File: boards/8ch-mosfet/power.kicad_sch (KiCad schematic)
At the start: 21 parts, among them J3 Screw_Terminal_01x08, J4 Screw_Terminal_01x08, U3 R-78K5.0-1.0

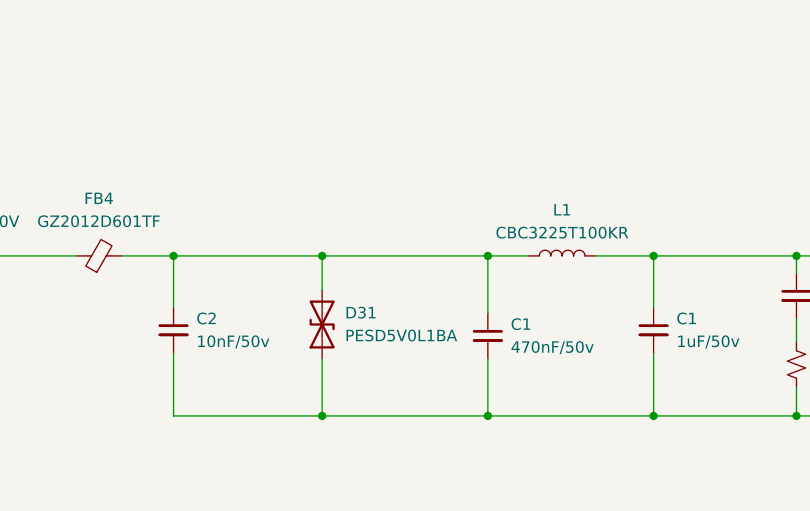
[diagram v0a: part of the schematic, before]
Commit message: added in reverse polarity diode to power circuit
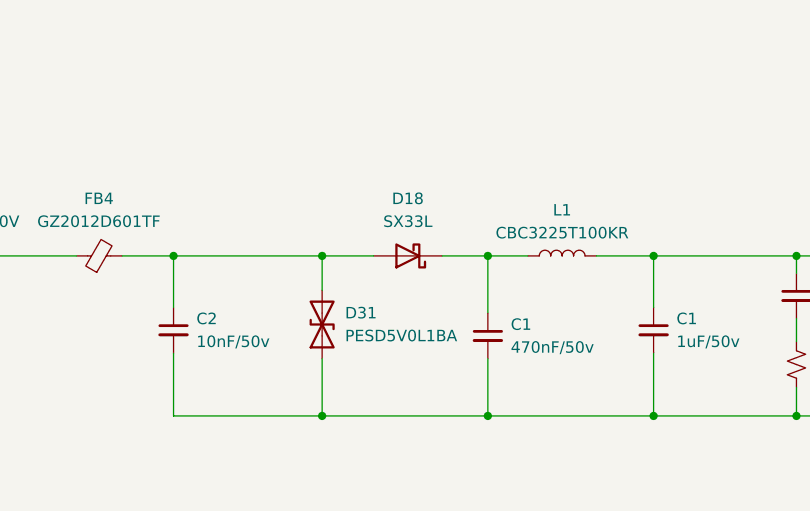
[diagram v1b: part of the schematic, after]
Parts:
- added D18: SX33L, Diode_SMD:D_SMA, symbol Device:D_Schottky
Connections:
- net at C2.1, D31.2 (A2), FB4.2: now also D18.2 (A); no longer C1.1, L1.1
- new net: C1.1, D18.1 (K), L1.1
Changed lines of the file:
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@@
+    (stroke (width 0) (type default))
+  )
+  (wire (pts (xy 87.63 78.74) (xy 92.71 78.74))
     (stroke (width 0) (type default))
   )
@@
     (stroke (width 0) (type default))
   )
-  (wire (pts (xy 74.295 78.74) (xy 92.71 78.74))
+  (wire (pts (xy 74.295 78.74) (xy 80.01 78.74))
     (stroke (width 0) (type default))
   )
@@
         )
       )
+    )
+  )
+  (symbol (lib_id "Device:D_Schottky") (at 83.82 78.74 180) (unit 1)
+    (in_bom yes) (on_board yes) (dnp no) (fields_autoplaced)
+    (property "Reference" "D18" (at 83.82 72.39 0)
+      (effects (font (size 1.27 1.27)))
+    )
+    (property "Value" "SX33L" (at 83.82 74.93 0)
+      (effects (font (size 1.27 1.27)))
+    )
+    (property "Footprint" "Diode_SMD:D_SMA" (at 83.82 78.74 0)
+      (effects (font (size 1.27 1.27)) hide)
+    )
+    (property "Datasheet" "~" (at 83.82 78.74 0)
+      (effects (font (size 1.27 1.27)) hide)
+    )
+    (property "Vendor" " 610-CMHSH5-2L" (at 83.82 78.74 90)
+      (effects (font (size 1.27 1.27)) hide)
+    )
+    (pin "1")
+    (pin "2")
+    (instances
+      (project "8ch-mosfet"
+        (path "/c83c6236-96e9-46ad-9d7a-9e2efa4a7966/0eec6767-666b-42c0-ba36-2a83c9caeade"
+          (reference "D18") (unit 1)
+        )
+        (path "/c83c6236-96e9-46ad-9d7a-9e2efa4a7966/ccdb1c25-8d0f-4f30-ab70-bbc1ecf3f6f7"
+          (reference "D19") (unit 1)
+        )
+        (path "/c83c6236-96e9-46ad-9d7a-9e2efa4a7966/1e692482-a022-407a-8cb5-d9a3b23521a6"
+          (reference "D20") (unit 1)
+        )
+        (path "/c83c6236-96e9-46ad-9d7a-9e2efa4a7966/5952e660-2bb6-45cf-b9ea-f7a7c2d0954e"
+          (reference "D21") (unit 1)
+        )
+        (path "/c83c6236-96e9-46ad-9d7a-9e2efa4a7966/772d44f5-8758-48db-a140-72ed8e75e88c"
+          (reference "D22") (unit 1)
+        )
+        (path "/c83c6236-96e9-46ad-9d7a-9e2efa4a7966/424e7b24-5644-46f2-85bb-1e459a343705"
+          (reference "D23") (unit 1)
+        )
+        (path "/c83c6236-96e9-46ad-9d7a-9e2efa4a7966/4c1df725-56ca-4be4-8107-a39054acbca4"
+          (reference "D24") (unit 1)
+        )
+        (path "/c83c6236-96e9-46ad-9d7a-9e2efa4a7966/a8a81147-5613-4820-beb3-a7ca76d0db8e"
+          (reference "D25") (unit 1)
+        )
+        (path "/c83c6236-96e9-46ad-9d7a-9e2efa4a7966"
+          (reference "D26") (unit 1)
+        )
+        (path "/c83c6236-96e9-46ad-9d7a-9e2efa4a7966/e112a34f-fd2f-43cb-bf5d-a7f5e57b6bef"
+          (reference "D38") (unit 1)
+        )
+      )

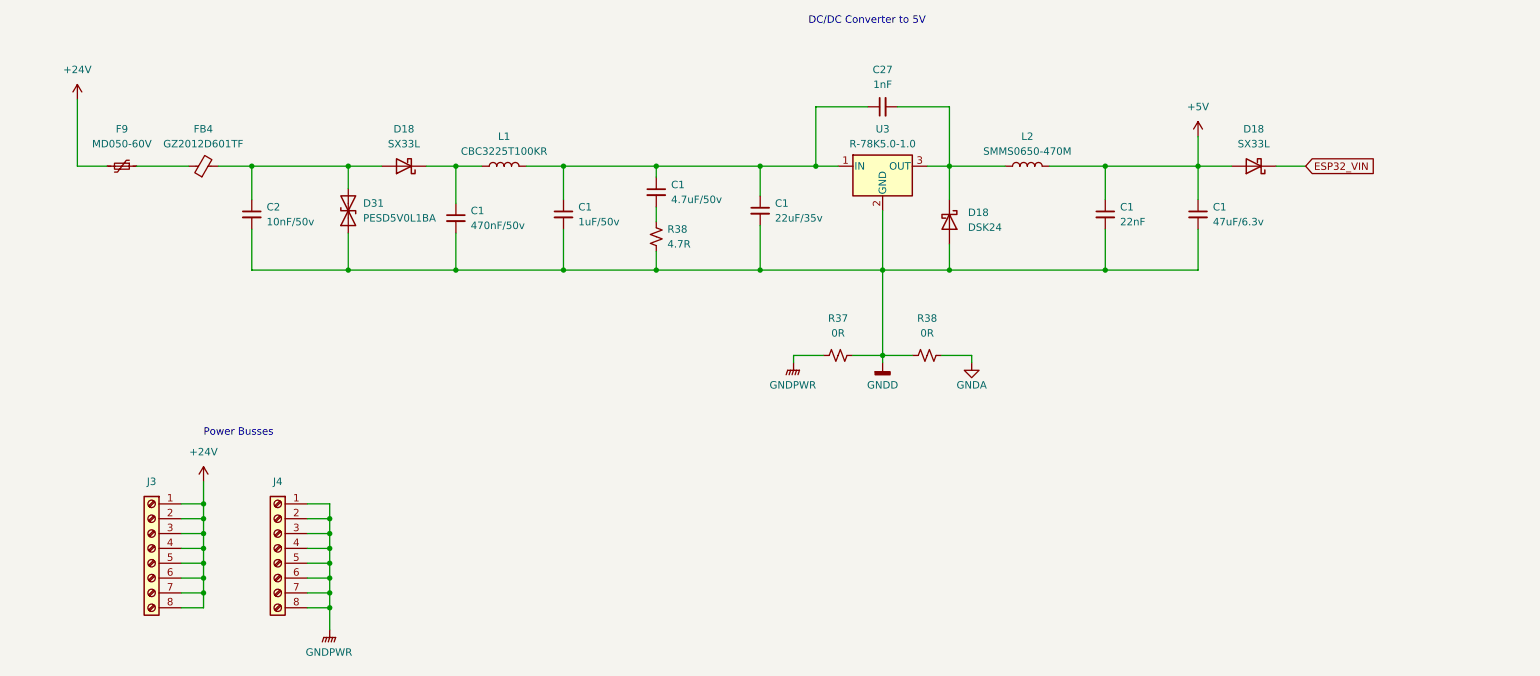
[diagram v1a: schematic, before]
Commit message: updated schematic to pass erc
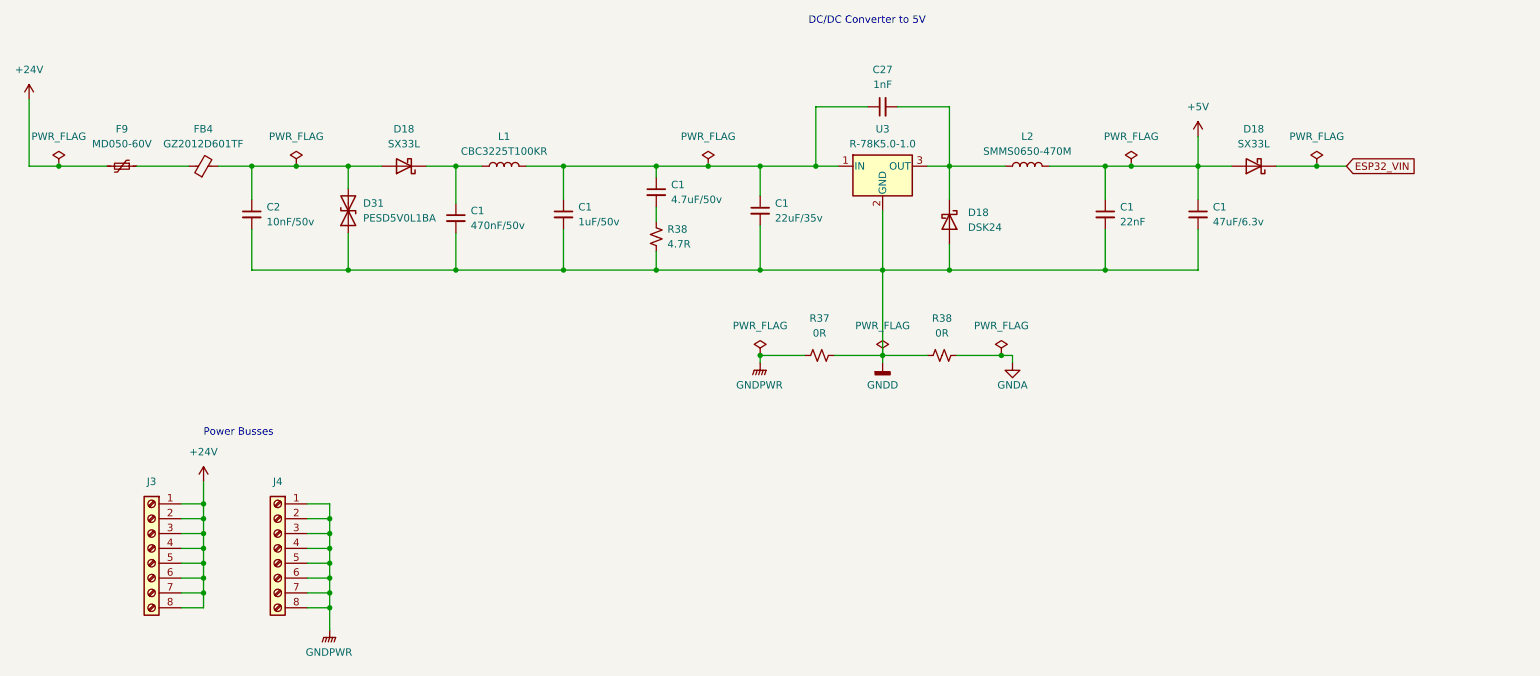
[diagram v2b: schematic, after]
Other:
- moved on the sheet: R37, R38

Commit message: tidied up the schematic
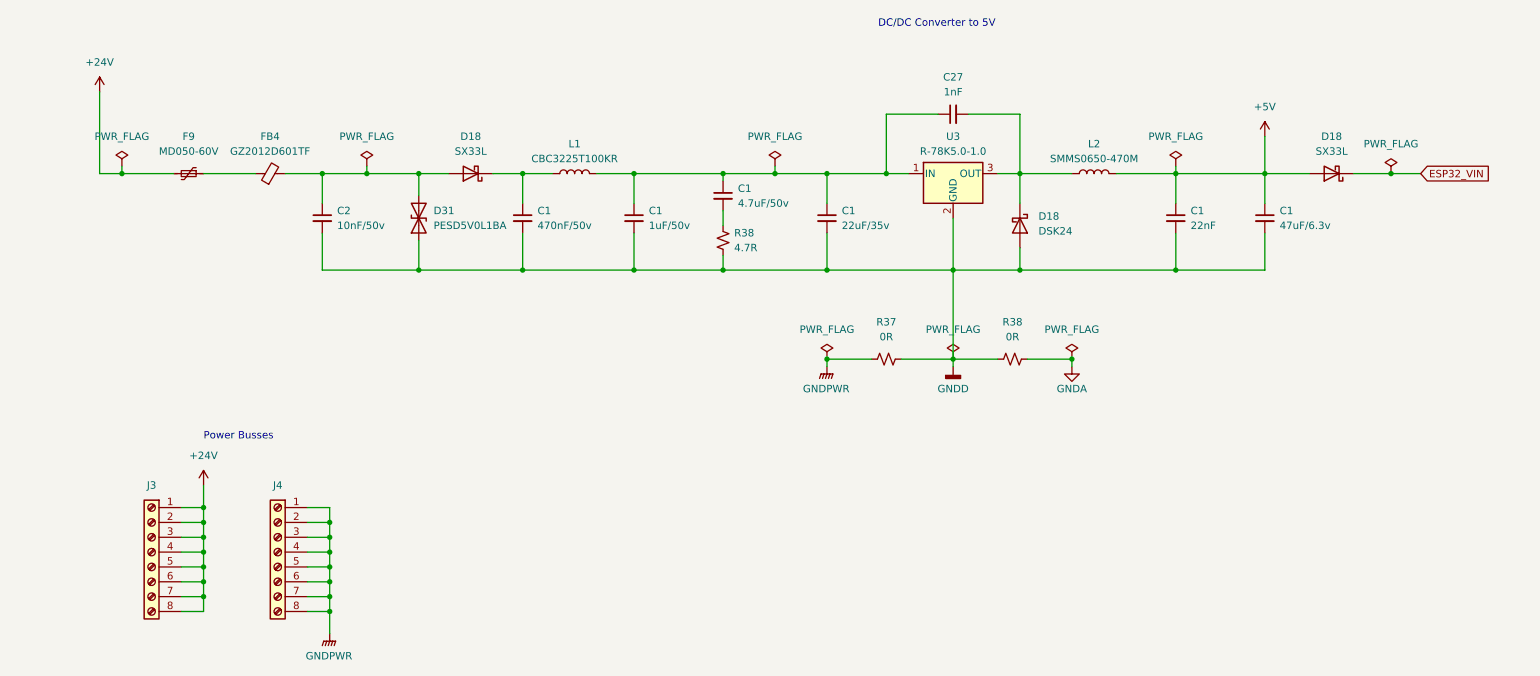
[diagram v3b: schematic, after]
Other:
- moved on the sheet: C1, C2, C27, D18, D31, F9, FB4, J3, J4, L1, L2, R37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

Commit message: tested the bus voltage stuff a bit more
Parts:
- D31: value PESD5V0L1BA -> SMBJ30CA; footprint Diode_SMD:D_SOD-323_HandSoldering -> Diode_SMD:D_SMB
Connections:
- net ESP32_VIN renamed ESP32_5V
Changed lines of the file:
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@@
     (effects (font (size 1.27 1.27)) (justify left bottom))
   )
-  (global_label "ESP32_VIN" (shape input) (at 257.81 80.01 0) (fields_autoplaced)
+  (global_label "ESP32_5V" (shape input) (at 257.81 80.01 0) (fields_autoplaced)
     (effects (font (size 1.27 1.27)) (justify left))
-    (property "Intersheetrefs" "${INTERSHEET_REFS}" (at 270.8342 80.01 0)
+    (property "Intersheetrefs" "${INTERSHEET_REFS}" (at 270.1084 80.01 0)
       (effects (font (size 1.27 1.27)) (justify left) hide)
     )
@@
       (effects (font (size 1.27 1.27)) (justify right))
     )
-    (property "Value" "PESD5V0L1BA" (at 88.9 88.9 90)
+    (property "Value" "SMBJ30CA" (at 88.9 88.9 90)
       (effects (font (size 1.27 1.27)) (justify right))
     )
-    (property "Footprint" "Diode_SMD:D_SOD-323_HandSoldering" (at 86.36 87.63 0)
-      (effects (font (size 1.27 1.27)) hide)
-    )
+    (property "Footprint" "Diode_SMD:D_SMB" (at 86.36 87.63 0)
+      (effects (font (size 1.27 1.27)) hide)
+    )

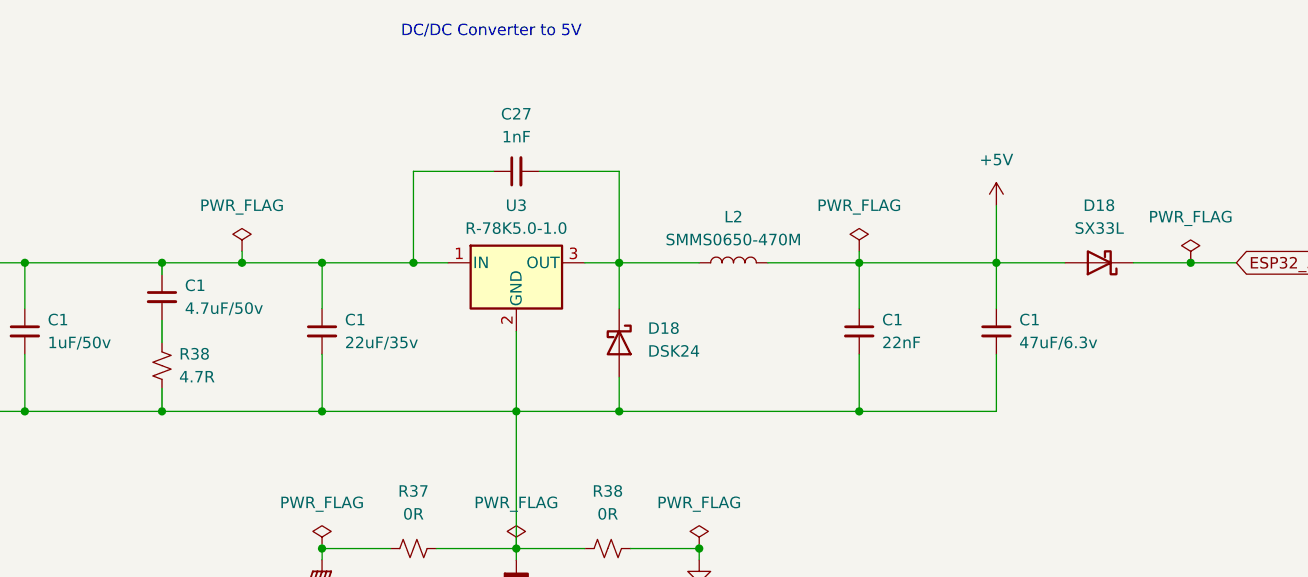
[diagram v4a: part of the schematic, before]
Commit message: changed voltage regulator to smt
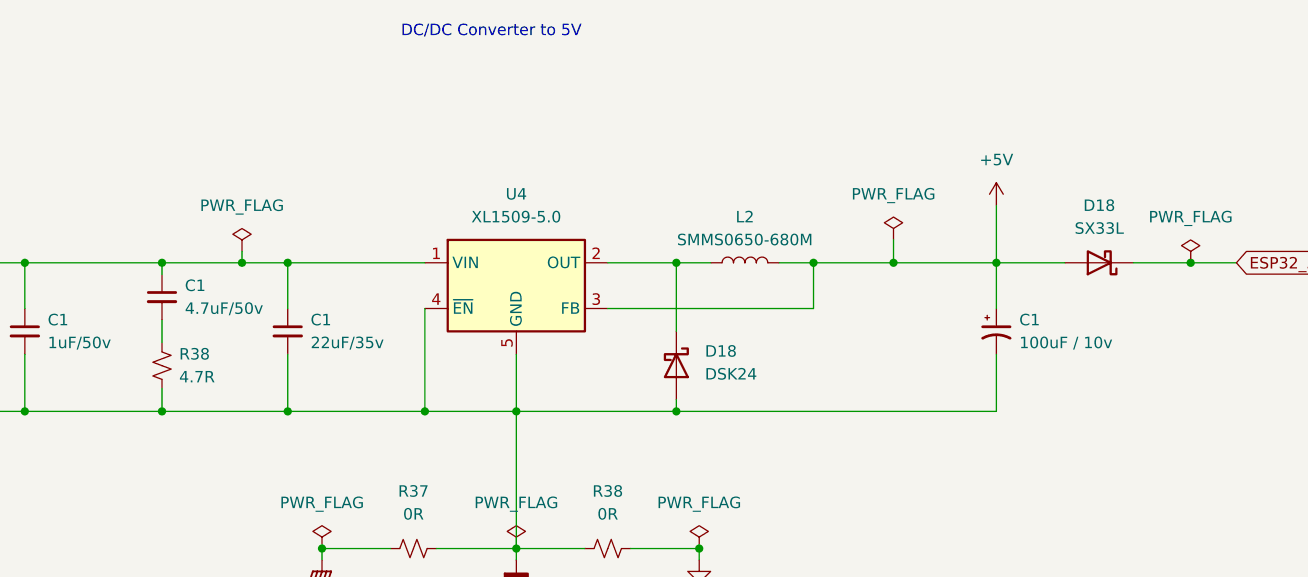
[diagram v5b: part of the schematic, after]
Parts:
- removed C1: 22nF, Capacitor_SMD:C_0805_2012Metric_Pad1.18x1.45mm_HandSolder, symbol Device:C_Small
- removed C27: 1nF, Capacitor_SMD:C_0805_2012Metric_Pad1.18x1.45mm_HandSolder, symbol Device:C_Small
- removed U3: R-78K5.0-1.0, gnarboard:RECOM R-78K, symbol Regulator_Switching:R-78B3.3-2.0
- added U4: XL1509-5.0, Package_SO:SOIC-8_3.9x4.9mm_P1.27mm, symbol Regulator_Switching:XL1509-5.0
- C1: value 47uF/6.3v -> 100uF / 10v; footprint Capacitor_SMD:C_0805_2012Metric_Pad1.18x1.45mm_HandSolder -> Capacitor_Tantalum_SMD:CP_EIA-3528-21_Kemet-B; symbol Device:C_Small -> Device:C_Polarized_Small_US; Vendor 08053C104KAT4A -> TAJC107K010RNJ
- L2: value SMMS0650-470M -> SMMS0650-680M
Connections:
- net +5V: now also U4.3 (FB)
- net GNDD: now also U4.4 (~{EN}), U4.5 (GND), U4.6 (GND), U4.7 (GND), U4.8 (GND)
- net at C1.1, C1.1, C1.1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: now also U4.1 (VIN)
- net at D18.1 (K), L2.1: now also U4.2 (OUT)
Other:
- moved on the sheet: C1, D18, L2

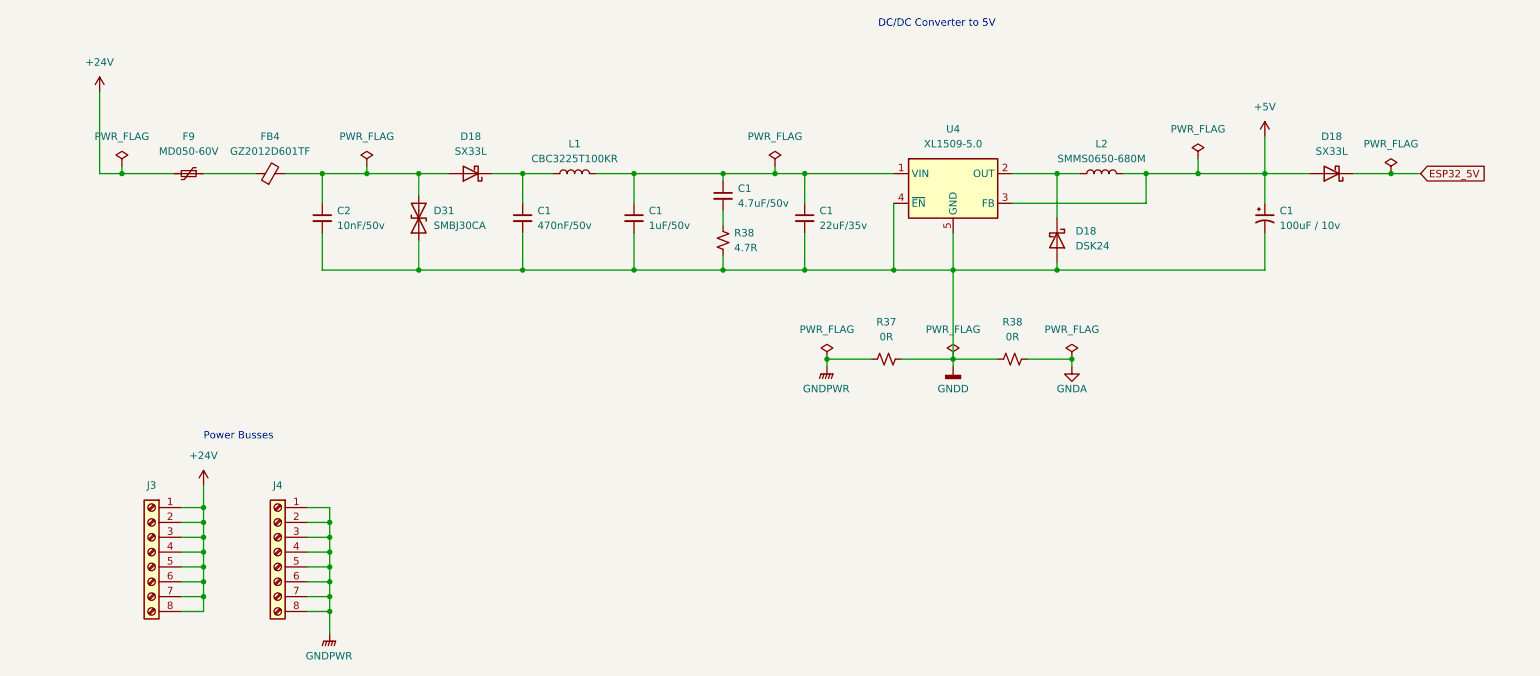
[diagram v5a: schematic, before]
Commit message: added 5v fuse to schematic
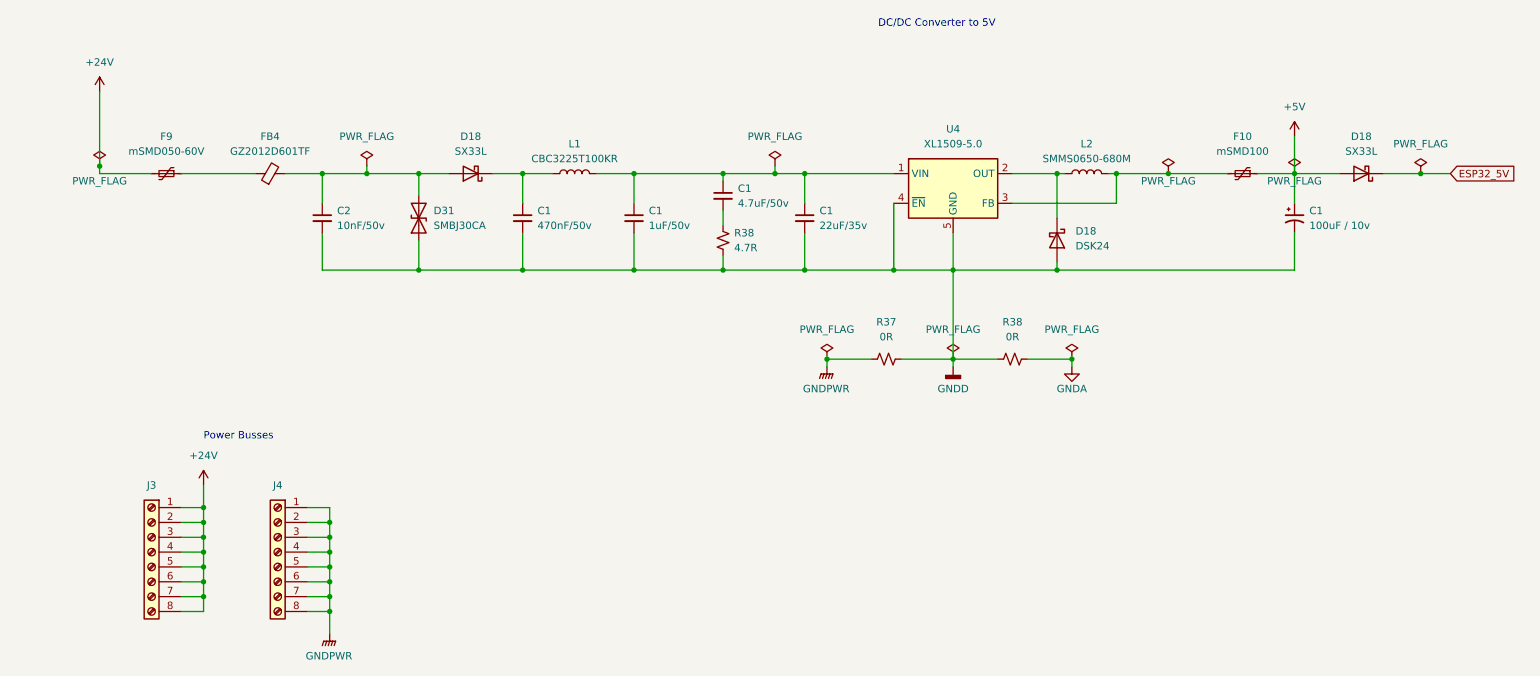
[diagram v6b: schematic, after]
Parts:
- added F10: mSMD100, Fuse:Fuse_1812_4532Metric_Pad1.30x3.40mm_HandSolder, symbol Device:Polyfuse_Small
- F9: value MD050-60V -> mSMD050-60V
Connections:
- net +5V: now also F10.1; no longer L2.2, U4.3 (FB)
- new net: F10.2, L2.2, U4.3 (FB)
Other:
- moved on the sheet: C1, D18, F9, L2

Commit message: updated layout with new fuse.
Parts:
- J3, J4: footprint gnarboard:Busbar 1x9 .375in -> yarrboard:Busbar 1x9 .375in
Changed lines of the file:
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@@
       (effects (font (size 1.27 1.27)) hide)
     )
-    (property "Footprint" "gnarboard:Busbar 1x9 .375in" (at 40.64 144.78 0)
+    (property "Footprint" "yarrboard:Busbar 1x9 .375in" (at 40.64 144.78 0)
       (effects (font (size 1.27 1.27)) hide)
     )
@@
       (effects (font (size 1.27 1.27)) hide)
     )
-    (property "Footprint" "gnarboard:Busbar 1x9 .375in" (at 62.23 144.78 0)
+    (property "Footprint" "yarrboard:Busbar 1x9 .375in" (at 62.23 144.78 0)
       (effects (font (size 1.27 1.27)) hide)
     )

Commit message: prepared 8ch mosfet for production
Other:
- company: (none) -> https://github.com/hoeken/yarrboard
- title: (none) -> Yarrboard 8ch Mosfet Driver
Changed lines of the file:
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@@
 (kicad_sch (version 20230121) (generator eeschema)
   (paper "A4")
+  (title_block
+    (title "Yarrboard 8ch Mosfet Driver")
+    (company "https://github.com/hoeken/yarrboard")
+  )
   (junction (at 177.8 111.76) (diameter 0) (color 0 0 0 0)
   )
